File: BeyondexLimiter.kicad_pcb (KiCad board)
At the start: 2 copper layers, 22.5 x 13 mm, 8 parts, among them U1 MIC2544-1YM

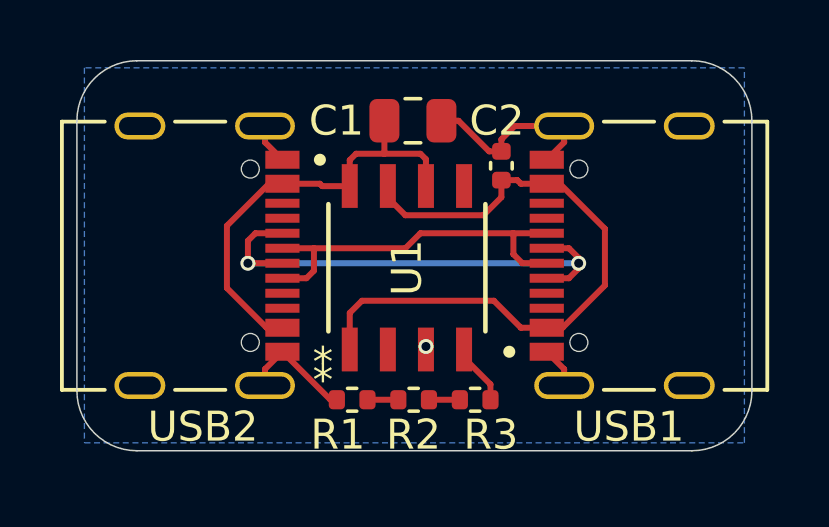
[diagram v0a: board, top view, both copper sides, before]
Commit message: Updated silkscreen with input/output labels for ports
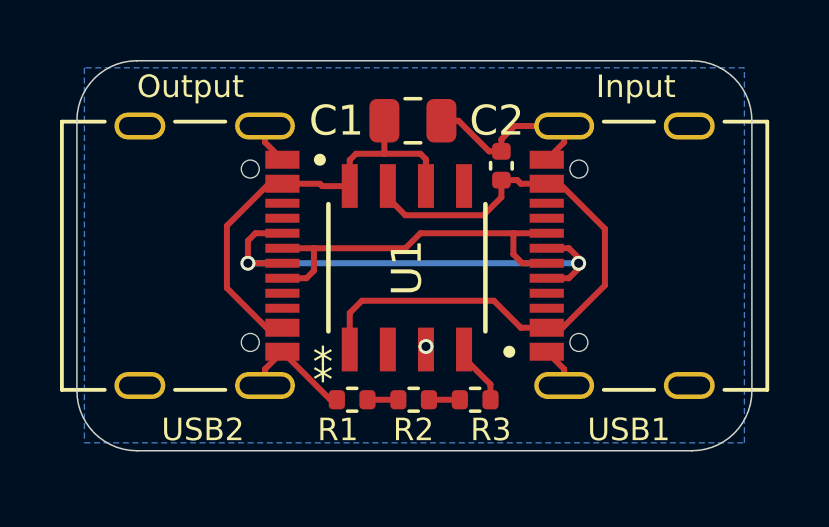
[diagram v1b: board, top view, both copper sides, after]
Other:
- board text added: "Input"
- board text added: "Input Upstream"
- board text added: "Output"
- board text added: "Output Downstream"
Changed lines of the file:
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@@
 		(tags "resistor")
 		(property "Reference" "R3"
-			(at -0.525 -1.16585 180)
-			(layer "F.SilkS")
-			(effects
-				(font
-					(size 1 1)
-					(thickness 0.15)
+			(at -0.525 -1 180)
+			(layer "F.SilkS")
+			(effects
+				(font
+					(size 0.75 0.75)
+					(thickness 0.1)
 				)
 			)
@@
 		(at 177.9125 97.5 90)
 		(property "Reference" "USB1"
-			(at -5.7 -2.0125 180)
-			(layer "F.SilkS")
-			(effects
-				(font
-					(size 1 1)
-					(thickness 0.15)
+			(at -5.8 -2.0125 180)
+			(layer "F.SilkS")
+			(effects
+				(font
+					(size 0.75 0.75)
+					(thickness 0.1)
 				)
 			)
@@
 		(at 159.6 97.5 -90)
 		(property "Reference" "USB2"
-			(at 5.7 -2.1 0)
-			(unlocked yes)
-			(layer "F.SilkS")
-			(effects
-				(font
-					(size 1 1)
-					(thickness 0.15)
+			(at 5.8 -2.1 0)
+			(unlocked yes)
+			(layer "F.SilkS")
+			(effects
+				(font
+					(size 0.75 0.75)
+					(thickness 0.1)
 				)
 			)
@@
 		(tags "resistor")
 		(property "Reference" "R1"
-			(at 0.475 -1.16585 180)
-			(layer "F.SilkS")
-			(effects
-				(font
-					(size 1 1)
-					(thickness 0.15)
+			(at 0.475 -1 180)
+			(layer "F.SilkS")
+			(effects
+				(font
+					(size 0.75 0.75)
+					(thickness 0.1)
 				)
 			)
@@
 		(tags "resistor")
 		(property "Reference" "R2"
-			(at 0.005 -1.16585 180)
-			(layer "F.SilkS")
-			(effects
-				(font
-					(size 1 1)
-					(thickness 0.15)
+			(at 0.005 -1 180)
+			(layer "F.SilkS")
+			(effects
+				(font
+					(size 0.75 0.75)
+					(thickness 0.1)
 				)
 			)
@@
 	)
 	(gr_line
+		(start 157.5 93)
+		(end 157.5 102)
+		(stroke
+			(width 0.05)
+			(type default)
+		)
+		(layer "Edge.Cuts")
+	)
+	(gr_arc
+		(start 157.5 93)
+		(mid 158.085786 91.585786)
+		(end 159.5 91)
+		(stroke
+			(width 0.05)
+			(type default)
+		)
+		(layer "Edge.Cuts")
+	)
+	(gr_arc
+		(start 159.5 104)
+		(mid 158.085786 103.414214)
+		(end 157.5 102)
+		(stroke
+			(width 0.05)
+			(type default)
+		)
+		(layer "Edge.Cuts")
+	)
+	(gr_line
 		(start 159.5 104)
 		(end 178 104)
@@
 		(start 178 91)
 		(end 159.5 91)
-		(stroke
-			(width 0.05)
-			(type default)
-		)
-		(layer "Edge.Cuts")
-	)
-	(gr_line
-		(start 180 102)
-		(end 180 93)
 		(stroke
 			(width 0.05)
@@
 	)
 	(gr_arc
-		(start 159.5 104)
-		(mid 158.085786 103.414214)
-		(end 157.5 102)
-		(stroke
-			(width 0.05)
-			(type default)
-		)
-		(layer "Edge.Cuts")
-	)
-	(gr_line
-		(start 157.5 93)
-		(end 157.5 102)
-		(stroke
-			(width 0.05)
-			(type default)
-		)
-		(layer "Edge.Cuts")
-	)
-	(gr_arc
 		(start 180 102)
 		(mid 179.414214 103.414214)
@@
 		(layer "Edge.Cuts")
 	)
-	(gr_arc
-		(start 157.5 93)
-		(mid 158.085786 91.585786)
-		(end 159.5 91)
+	(gr_line
+		(start 180 102)
+		(end 180 93)
 		(stroke
 			(width 0.05)
@@
 	)
 	(gr_line
-		(start 169.2 109.07)
-		(end 169.2 110.7)
+		(start 160.9 110.3)
+		(end 160.9 108.84)
+		(stroke
+			(width 0.1)
+			(type default)
+		)
+		(layer "User.1")
+	)
+	(gr_line
+		(start 162.42 110)
+		(end 159.3 110)
 		(stroke
 			(width 0.1)
@@
 	)
 	(gr_line
-		(start 162.42 110)
-		(end 159.3 110)
+		(start 169.2 109.07)
+		(end 169.2 110.7)
 		(stroke
 			(width 0.1)
@@
 		(layer "User.1")
 	)
-	(gr_line
-		(start 160.9 110.3)
-		(end 160.9 108.84)
-		(stroke
-			(width 0.1)
-			(type default)
-		)
-		(layer "User.1")
+	(gr_text "Output"
+		(at 159.5 92.3 0)
+		(layer "F.SilkS")
+		(effects
+			(font
+				(size 0.75 0.75)
+				(thickness 0.1)
+			)
+			(justify left bottom)
+		)
+	)
+	(gr_text "Input"
+		(at 174.8 92.3 0)
+		(layer "F.SilkS")
+		(effects
+			(font
+				(size 0.75 0.75)
+				(thickness 0.1)
+			)
+			(justify left bottom)
+		)
 	)
 	(gr_text "Beyondex Current Limiter\nUSB 2.0 200mA Limit\nv0.1 Designed by Kibbie"
@@
 		)
 	)
+	(gr_text "Output\nDownstream"
+		(at 160 97.5 90)
+		(layer "B.SilkS")
+		(effects
+			(font
+				(size 0.75 0.75)
+				(thickness 0.1)
+			)
+			(justify bottom mirror)
+		)
+	)
+	(gr_text "Input\nUpstream"
+		(at 177.6 97.5 270)
+		(layer "B.SilkS")
+		(effects
+			(font
+				(size 0.75 0.75)
+				(thickness 0.1)
+			)
+			(justify bottom mirror)
+		)
+	)

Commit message: Bump version so I can post another release
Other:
- board text added: "Beyondex Current Limiter USB 2.0 200mA Limit v0.2 Designed by Kibbie"
- board text removed: "Beyondex Current Limiter USB 2.0 200mA Limit v0.1 Designed by Kibbie"
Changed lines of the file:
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@@
 		)
 	)
-	(gr_text "Beyondex Current Limiter\nUSB 2.0 200mA Limit\nv0.1 Designed by Kibbie"
+	(gr_text "Beyondex Current Limiter\nUSB 2.0 200mA Limit\nv0.2 Designed by Kibbie"
 		(at 168.8 97.5 0)
 		(layer "B.SilkS")
